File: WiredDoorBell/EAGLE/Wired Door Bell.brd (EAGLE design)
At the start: 75 x 40 mm, 12 parts, among them T1 2N2222

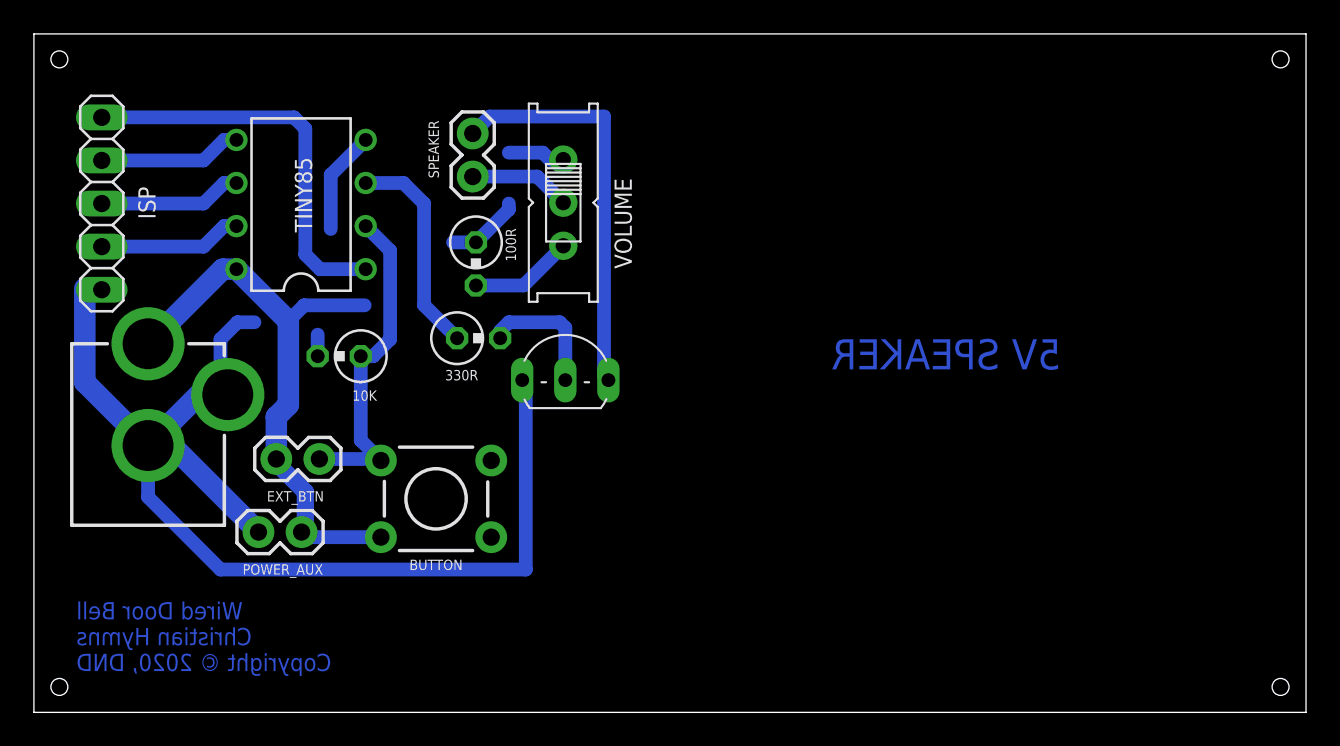
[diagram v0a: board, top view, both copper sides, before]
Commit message: Eagle : Fixed Schematics, Board and PCB
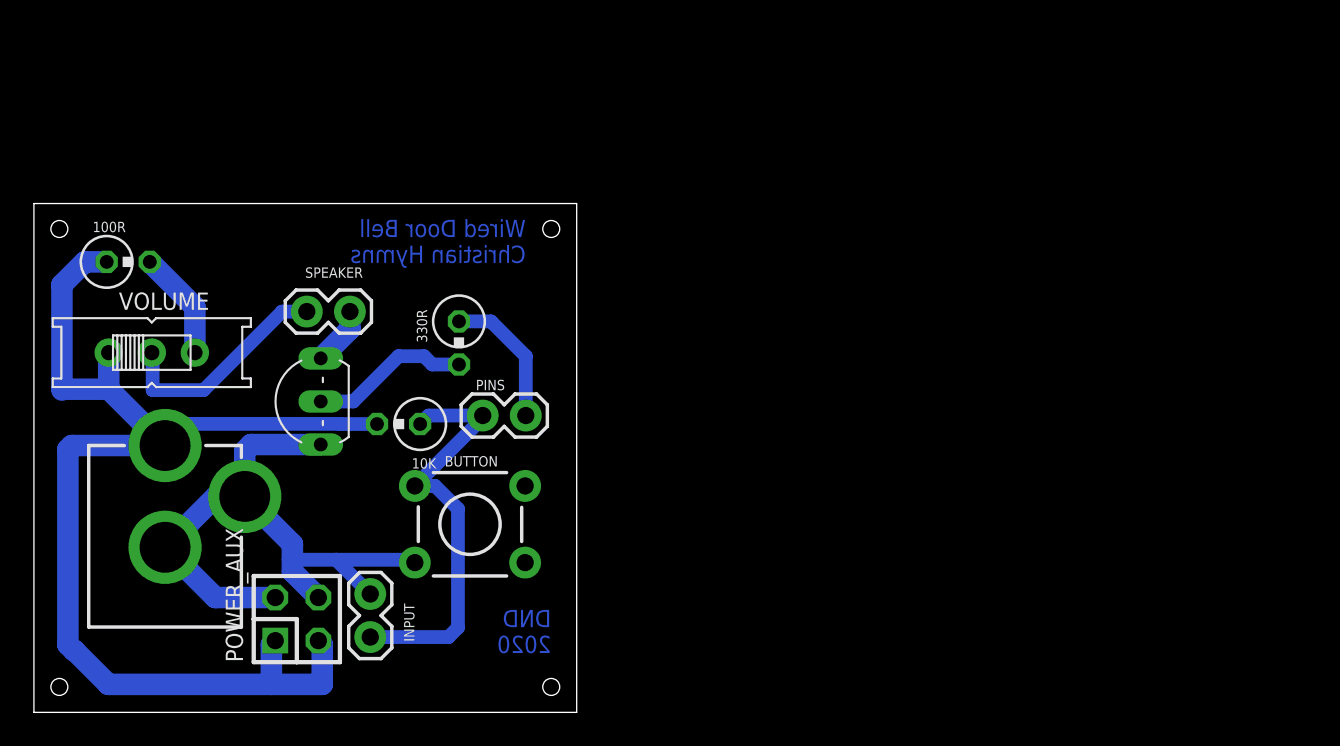
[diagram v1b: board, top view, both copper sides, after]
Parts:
- removed EXT_BTN: (no value), SparkFun-Connectors:1X02
- removed ISP: (no value), pinhead:1X05
- removed TINY85: ATTINY85-20P, _hhn_attiny25_45_85:PDIP08_300MIL
- added INPUT, PINS: (no value), SparkFun-Connectors:1X02
- POWER_AUX: value (none) -> F-2X02-DIL-100; device SparkFun-Connectors:1X02 -> con-headers-jp:DIL-100-2X02
- moved VOLUME 25.8 mm to (6.95, 21.2), turned to 0 degrees
- moved 100R 20.5 mm to (5.56, 26.6), turned to 0 degrees
- moved T1 15.9 mm to (15.6, 18.3), turned to 90 degrees
- moved SPEAKER 12.8 mm to (18.6, 23.6), turned to 180 degrees
- moved POWER 6.08 mm to (7.73, 2.03)
- moved 10K 5.32 mm to (21.5, 17.0)
- moved POWER_AUX 5.14 mm to (15.5, 5.50), turned to 0 degrees
- moved BUTTON 2.50 mm to (25.7, 11.1)
- moved 330R 1.19 mm to (25.1, 21.8), turned to 270 degrees
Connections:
- net SPK_5V renamed SPK_VOL
- removed net NRESET: ISP.5, TINY85.1
- removed net P0_MOSI: ISP.4, TINY85.5
- removed net P1_MISO: ISP.3, TINY85.6
- removed net P2_SCK: ISP.2, TINY85.7
- net 5V: now also 10K.2, POWER_AUX.3; no longer BUTTON.3, EXT_BTN.2, TINY85.8
- net BTN_IN: now also INPUT.1, PINS.2; no longer EXT_BTN.1, TINY85.2
- net GND: now also BUTTON.3, INPUT.2, POWER_AUX.4; no longer 10K.2, ISP.1, TINY85.4
- net SPK_PWM: now also PINS.1; no longer TINY85.3
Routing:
- net GND: track 78.0 -> 38.9 mm
- net 5V: track 43.8 -> 70.7 mm
- net NRESET: track 23.6 -> 0.00 mm
- net SPK_GND: track 23.8 -> 3.47 mm
- net P2_SCK: track 8.44 -> 0.00 mm
- net P1_MISO: track 8.44 -> 0.00 mm
- net P0_MOSI: track 8.44 -> 0.00 mm
- net SPK_VOL: track 5.98 -> 13.5 mm
- net BTN_IN: track 19.7 -> 25.2 mm
- net SPK_PWM: track 12.7 -> 8.29 mm
- net SPK_SIG: track 7.70 -> 9.46 mm
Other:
- board size 75 x 40 mm -> 32 x 30 mm
- board text added: "DND 2020"
- board text added: "Wired Door Bell Christian Hymns"
- board text removed: "5V SPEAKER"
- board text removed: "Wired Door Bell Christian Hymns Copyright © 2020, DND"
